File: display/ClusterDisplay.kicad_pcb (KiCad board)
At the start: 4 copper layers, 125.4 x 106 mm, 117 parts, among them J1 Verdin iMX95 Hexa 8GB WB IT, J10 RTC coin cell, J11 Molex KK-254 22-27-2041, rota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, J2 Phoenix MKDS 1,5/3-5,08 power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, J3 Molex KK-254 22-27-2031 priva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, J4 TST040HDBC-42 panel, J8 Samtec TSW-108-07-G-S JTAG (b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, J9 Samtec TSW-104-07-G-S buttons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, Q1 PMV55ENEA (AEC-Q101, 60V/20V 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, Q2 PMV55ENEA (AEC-Q101, 60V/20V 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, Q3 PMV55ENEA ignition wake pulld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, U1 LM74930-Q1, U2 LM61460-Q1, U3 TLV767-Q1, U4 TCAN1044V-Q1, U6 TPS65131-Q1, U7 TPS61165-Q1, U8 TPS22918-Q1 (AEC-Q100 G2) dia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

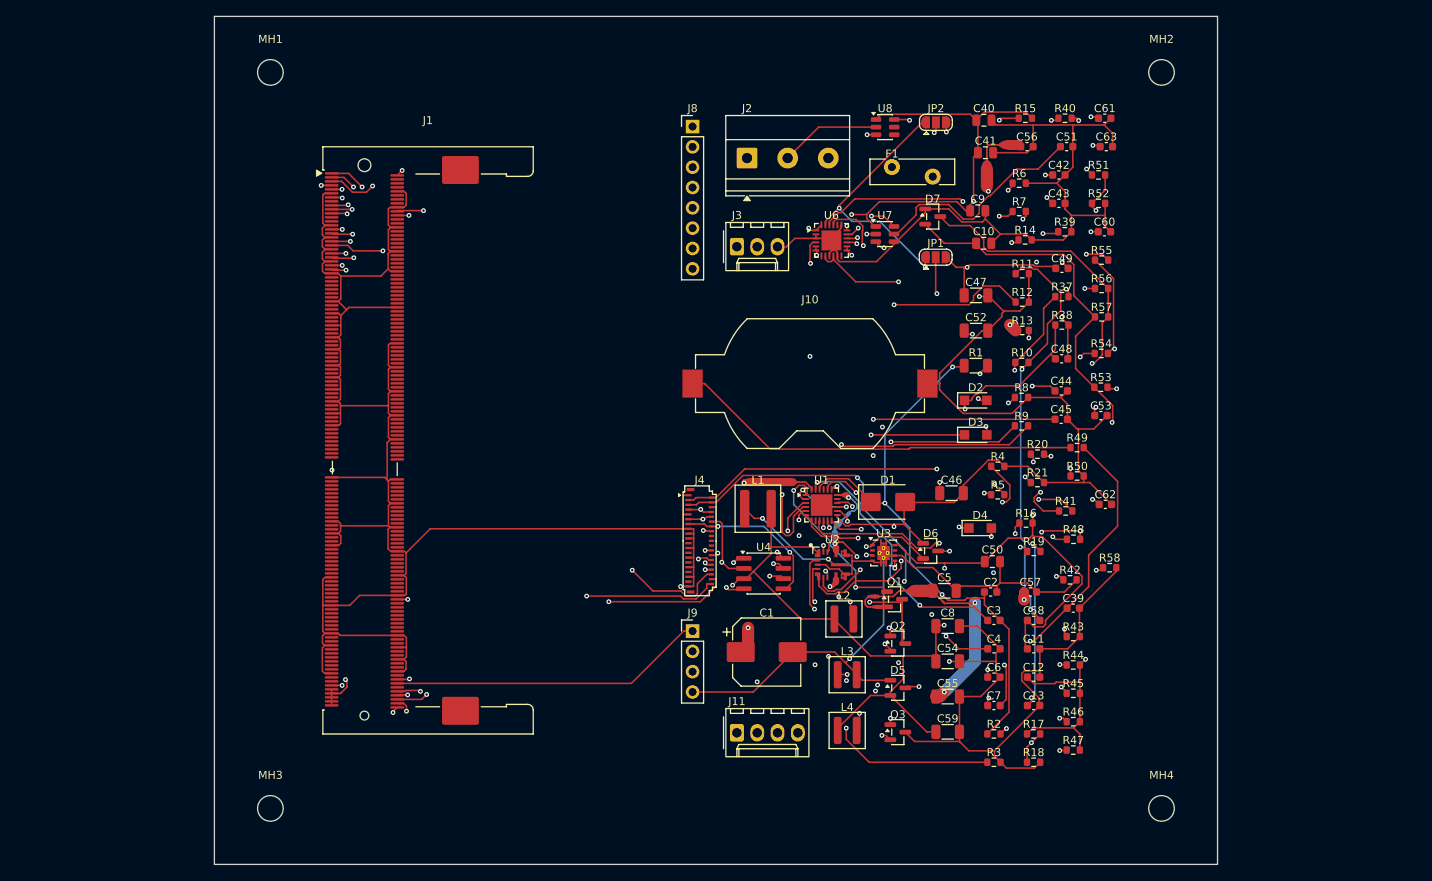
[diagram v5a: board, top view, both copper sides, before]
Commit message: Fix review findings: MOSFET pinout, gauges surge front end, converter cells, DSI
Review of 2026-10-03 found real defects; fixes and measured results:
- Nexperia PMV55ENEA/PMV37ENEA pinout is G=1, S=2, D=3: display Q1-Q3 and
  gauges Q2 had source/drain swapped. Fixed in both schematics.
- gauges/ now has the same LM74930-Q1 surge-protected front end as display/
  (5 mohm sense, OV clamp), a 5 A/32 V blade fuse on display/ (the MF-RG500 PTC
  was a 16 V part), and sender inputs with series resistor, clamp and filter.
- Converters are placed as cells around their ICs (tools/cellplace.py).
  display: SW_5V 55.6 -> 11.6 mm, boost/inverter/backlight SW 75 -> 7-13 mm,
  LM61460 input caps 57 -> 4.7-7.5 mm. gauges: SW 26.8 -> 8.7 mm, input caps 4.5 mm.
- display DSI pairs are planned by dsi_route.py after the autorouter: legs
  10.6-11.2 mm, at most 0.6 mm skew in a pair (was 64-85 mm, 21 mm skew).
- In1 is a GND plane for the router on display/ (about 925 mm of slow signals
  still cross it, down from 2615); forbidding signals there left 6-122
  connections unrouted. gauges/ keeps the old flow (planes claimed there made
  the real GND zone split into islands).
- display: USB (J13) and console UART (J12) bring-up headers, SoM and socket
  split into separate BOM lines, README rewritten.
- gauges: orderable MCU part number, DNP parts get their own BOM line and are
  left out of the placement file, 5 mohm sense resistor in the catalog.

Both boards: 0 unconnected, independent kicad-cli DRC with only accepted
categories; fab packages rebuilt. Nothing is fabricated or tested.

Co-Authored-By: Claude Sonnet 5.5 <noreply@anthropic.com>
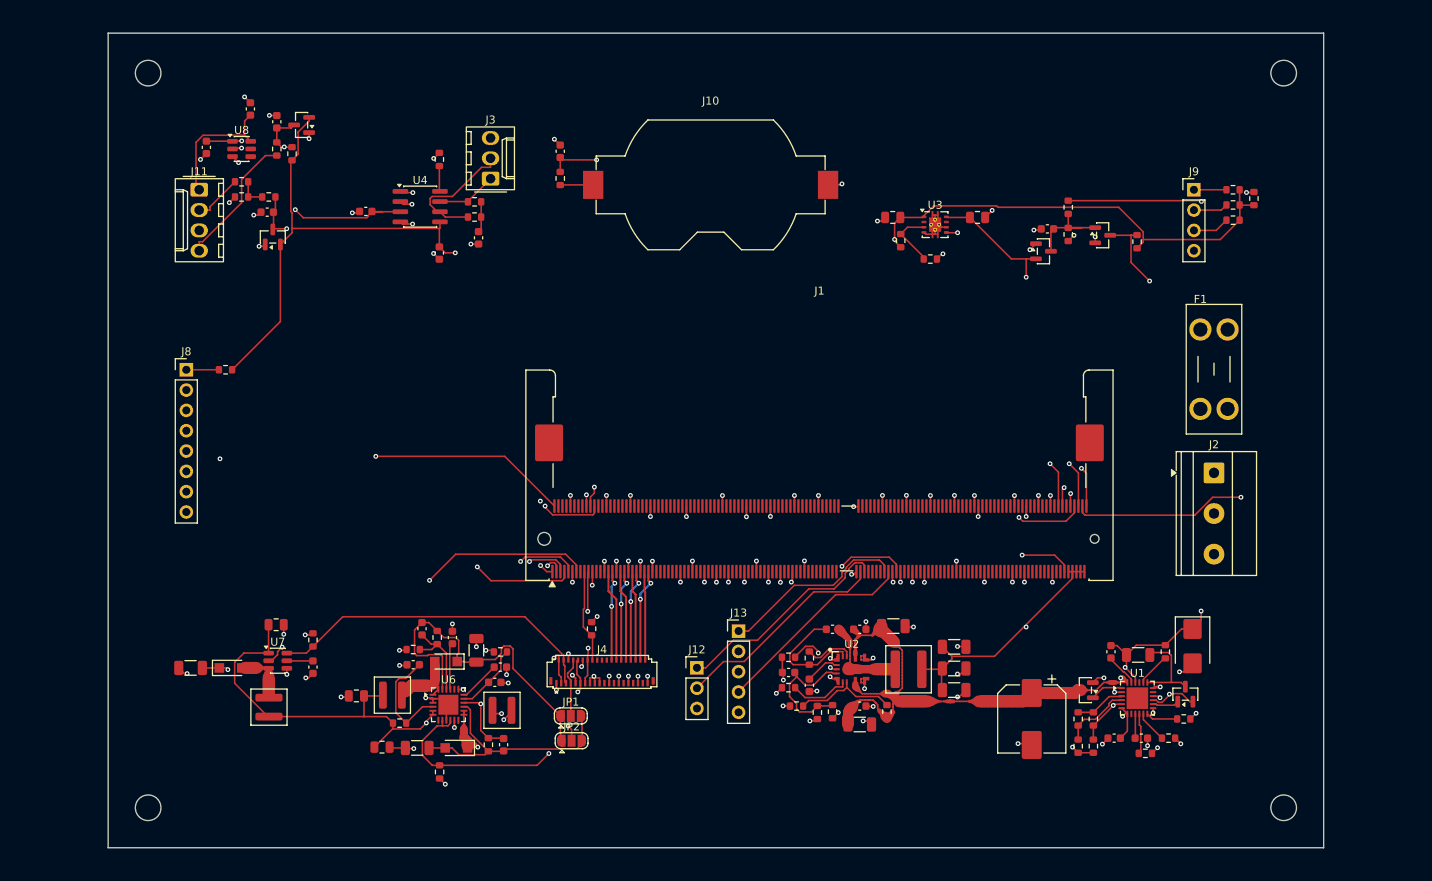
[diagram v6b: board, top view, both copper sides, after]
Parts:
- added J12: Samtec TSW-103-07-G-S A55 console UART_3 1.8V (bench only), Connector_PinHeader_2.54mm:PinHeader_1x03_P2.54mm_Vertical, F.Cu at (207.6, 176.9)
- added J13: Samtec TSW-105-07-G-S USB_1 OTG (bench only), Connector_PinHeader_2.54mm:PinHeader_1x05_P2.54mm_Vertical, F.Cu at (212.8, 172.3)
- F1: value MF-RG500 (Bourns, 5.0A hold/8.5A trip, AEC-Q200) -> Keystone 3568 holder, 5A Littelfuse 0297005.WXNV MINI blade fuse (32V, 1kA); footprint Fuse:Fuse_Bourns_MF-RG500 -> Fuse:Fuseholder_Blade_Mini_Keystone_3568
- moved R58 118.0 mm to (150.7, 118.1), turned to 180 degrees
- moved C51 114.5 mm to (159.6, 176.8), turned to -90 degrees
- moved C62 114.1 mm to (155.1, 108.7), turned to 90 degrees
- moved C60 112.8 mm to (146.3, 111.9), turned to -90 degrees
- moved R54 109.6 mm to (150.7, 116.2)
- moved R48 108.1 mm to (148.7, 139.7)
- moved C63 107.1 mm to (151.8, 107.1), turned to 90 degrees
- moved C52 106.8 mm to (144.3, 176.9), turned to 180 degrees
- moved C40 106.4 mm to (165.1, 180.4), turned to 180 degrees
- moved R40 106.4 mm to (181.6, 186.5), turned to 90 degrees
- moved C41 105.9 mm to (168.3, 186.8)
- moved C61 105.3 mm to (153.9, 120.0), turned to 180 degrees
- moved R56 104.6 mm to (155.1, 112.1), turned to 90 degrees
- moved R55 104.4 mm to (154.1, 118.1)
- moved R57 103.2 mm to (157.0, 112.7), turned to 90 degrees
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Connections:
- J1 pad 147: (no net) -> UART_RXD
- J1 pad 149: (no net) -> UART_TXD
- J1 pad 159: (no net) -> USB_VBUS
- J1 pad 161: (no net) -> USB_ID
- J1 pad 163: (no net) -> USB_DN
- J1 pad 165: (no net) -> USB_DP
- Q1 pad 2: +12V_PROT -> COMMON
- Q1 pad 3: COMMON -> +12V_PROT
- Q2 pad 2: SENSE_OUT -> COMMON
- Q2 pad 3: COMMON -> SENSE_OUT
- Q3 pad 2: IGN_WAKE_N -> GND
- Q3 pad 3: GND -> IGN_WAKE_N
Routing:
- net GND: track 760.2 -> 156.8 mm, vias 6 -> 120
- net +12V_PROT: track 190.1 -> 72.9 mm, vias 11 -> 2
- net DIAL_ADC: track 171.7 -> 63.8 mm, vias 4 -> 2
- net DSI_PANEL_EN: track 116.2 -> 11.6 mm, vias 3 -> 0
- net PANEL_BIAS_EN: track 149.8 -> 49.3 mm, vias 4 -> 2
- net DIAL_5V: track 113.1 -> 16.4 mm, vias 2 -> 0
- net DIAL_SIG_RAW: track 86.2 -> 6.18 mm, vias 2 -> 0
- net IGN_WAKE_N: track 122.1 -> 42.3 mm, vias 3 -> 2
- net JTAG_VREF: track 142.1 -> 63.2 mm, vias 3 -> 1
- net DSI_D2_N: track 85.4 -> 11.0 mm, vias 3 -> 0
- net CAN1_H: track 80.6 -> 7.58 mm, vias 2 -> 0
- net CAN1_L: track 88.5 -> 16.4 mm, vias 2 -> 0
- net IGN_GATE: track 83.4 -> 11.6 mm, vias 4 -> 0
- net BL_SW: track 76.6 -> 7.06 mm, vias 3 -> 0
- net PANEL_FBN: track 84.8 -> 16.8 mm, vias 4 -> 2
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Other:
- board size 125.4 x 106 mm -> 151.9 x 101.8 mm

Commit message: display: audio path, USB-C host port and wireless-radio notes for wireless Android Auto / CarPlay
Owner decision 2026-10-16: wireless Android Auto and CarPlay with sound.

- Audio: TI TAC5112-Q1 codec (real datasheet SLASFC2A, 1.8 V I/O so no level
  shifters, no MCLK) on Verdin I2S_1 + I2C_1, 3.3 V AVDD LDO, balanced stereo
  line-out J14, electret mic J15, TPD4E05U06-Q1 ESD, reserved DNP/TBD MFi
  coprocessor access header J16 (no Apple part invented).
- USB: USB-C 2.0 host J17 on Verdin USB_2, TPS2557-Q1 VBUS switch (1.6-2.0 A),
  22k Rp (1.5 A), ESD, VBUS TVS, EN pull-down. J13 stays the bench header.
- verdin_x1: I2S_1, I2C_1 and USB_2 moved out of the unused bank; verify() updated.
- Floorplan: audio column in the left strip, connector/ESD cell leads the top
  row, USB-C cell on the bottom edge. 151.9 -> 169.3 mm wide, same height.
- Routing: 0 unconnected nets (real kicad-cli DRC); B.Cu GND pour added to stop
  In1 islands from isolating GND vias; in-place retries cut, pipeline retries up.
- cellplace: optional keepin and anchor_gap per cell.
- BOM, fab package, README, fab README, PLAN decision 6 and docs/audio-and-usb.md
  (wiring, unbalanced AUX use, antenna rules, software bring-up, unverified list).

Co-Authored-By: Claude Sonnet 5.5 <noreply@anthropic.com>
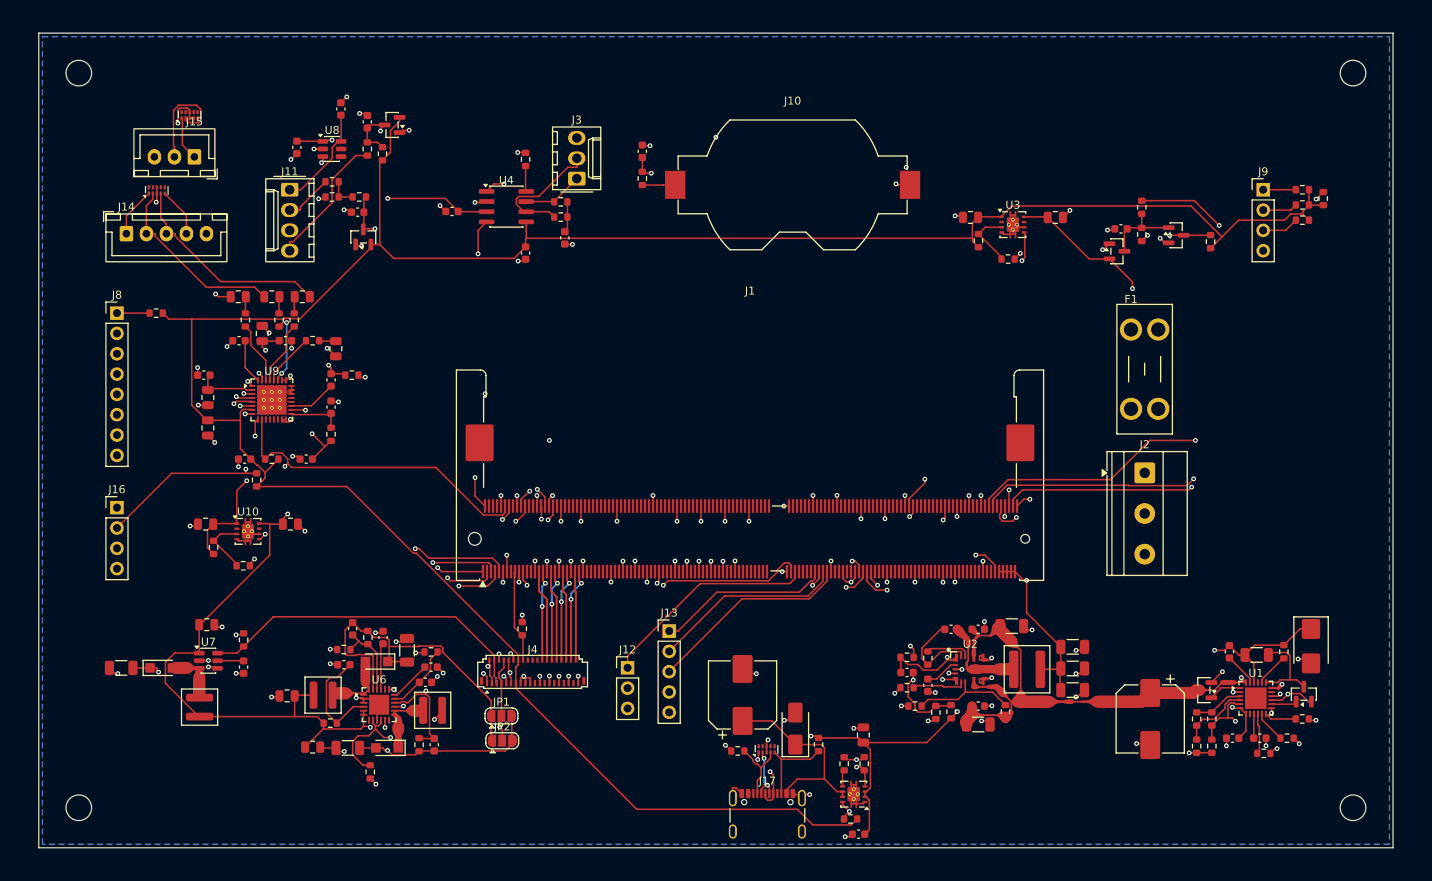
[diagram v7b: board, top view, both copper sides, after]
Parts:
- added C64: 10u CIN, Capacitor_SMD:C_0805_2012Metric, F.Cu at (156.8, 159.0)
- added C65: 10u COUT, Capacitor_SMD:C_0805_2012Metric, F.Cu at (146.2, 159.0)
- added C66: 10u AVDD, Capacitor_SMD:C_0805_2012Metric, F.Cu at (153.3, 135.1)
- added C67: 100n AVDD, Capacitor_SMD:C_0603_1608Metric, F.Cu at (156.2, 136.0)
- added C68: 10u DREG, Capacitor_SMD:C_0805_2012Metric, F.Cu at (146.5, 143.1)
- added C69: 100n DREG, Capacitor_SMD:C_0603_1608Metric, F.Cu at (146.0, 140.3)
- added C70: 10u IOVDD, Capacitor_SMD:C_0805_2012Metric, F.Cu at (146.5, 146.9)
- added C71: 100n IOVDD, Capacitor_SMD:C_0603_1608Metric, F.Cu at (151.1, 150.8)
- added C72: 1u VREF, Capacitor_SMD:C_0603_1608Metric, F.Cu at (150.4, 136.0)
- added C73: 1u MICBIAS, Capacitor_SMD:C_0603_1608Metric, F.Cu at (161.9, 144.3)
- added C74: 1u mic AC couple, Capacitor_SMD:C_0603_1608Metric, F.Cu at (158.8, 150.8)
- added C75: 1u mic AC couple, Capacitor_SMD:C_0603_1608Metric, F.Cu at (161.9, 140.9)
- added C76: 4.7u line-out DC block, Capacitor_SMD:C_0805_2012Metric, F.Cu at (162.5, 137.0)
- added C77: 4.7u line-out DC block, Capacitor_SMD:C_0805_2012Metric, F.Cu at (154.5, 130.5)
- added C78: 4.7u line-out DC block, Capacitor_SMD:C_0805_2012Metric, F.Cu at (158.3, 130.5)
- added C79: 4.7u line-out DC block, Capacitor_SMD:C_0805_2012Metric, F.Cu at (150.3, 130.5)
- added C80: 100n USB switch IN, Capacitor_SMD:C_0603_1608Metric, F.Cu at (227.8, 197.7)
- added C81: 10u USB switch IN, Capacitor_SMD:C_0805_2012Metric, F.Cu at (228.4, 185.3)
- added C82: 100u 35V hybrid polymer VBUS (Panasonic EEH-ZA1V101P), Capacitor_SMD:CP_Elec_8x10, F.Cu at (213.3, 180.3)
- added D8: SMAJ5.0A VBUS TVS, Diode_SMD:D_SMA, F.Cu at (219.9, 184.5)
- added J14: JST XH B5B-XH-A balanced line-out L/R, Connector_JST:JST_XH_B5B-XH-A_1x05_P2.50mm_Vertical, F.Cu at (136.3, 122.7)
- added J15: JST XH B3B-XH-A electret microphone (2-wire + shield), Connector_JST:JST_XH_B3B-XH-A_1x03_P2.50mm_Vertical, F.Cu at (144.8, 113.1)
- added J16: MFi coprocessor access I2C_1 + reset (TBD, DNP), Connector_PinHeader_2.54mm:PinHeader_1x04_P2.54mm_Vertical, F.Cu at (135.1, 156.9)
- added J17: GCT USB4105-GF-A USB-C 2.0 host receptacle, Connector_USB:USB_C_Receptacle_GCT_USB4105-xx-A_16P_TopMnt_Horizontal, F.Cu at (216.4, 196.3)
- added R59: 316k 1% FB top, Resistor_SMD:R_0603_1608Metric, F.Cu at (147.2, 161.9)
- added R60: 100k FB bot, Resistor_SMD:R_0603_1608Metric, F.Cu at (150.9, 164.2)
- added R61: 2.2k I2C1 SDA pull-up, Resistor_SMD:R_0603_1608Metric, F.Cu at (154.5, 150.8)
- added R62: 2.2k I2C1 SCL pull-up, Resistor_SMD:R_0603_1608Metric, F.Cu at (152.6, 153.4)
- added R63: 2.2k mic bias, Resistor_SMD:R_0603_1608Metric, F.Cu at (161.9, 147.7)
- added R64: 100R mic return, Resistor_SMD:R_0603_1608Metric, F.Cu at (164.5, 140.3)
- added R65: 100R line-out series, Resistor_SMD:R_0603_1608Metric, F.Cu at (159.6, 136.0)
- added R66: 100R line-out series, Resistor_SMD:R_0603_1608Metric, F.Cu at (155.4, 133.4)
- added R67: 100R line-out series, Resistor_SMD:R_0603_1608Metric, F.Cu at (157.3, 133.4)
- added R68: 100R line-out series, Resistor_SMD:R_0603_1608Metric, F.Cu at (151.2, 133.4)
- added R69: 61.9k 1% USB ILIM (1.6-2.0 A), Resistor_SMD:R_0603_1608Metric, F.Cu at (226.0, 188.9)
- added R70: 100k FAULT pull-up to +1V8, Resistor_SMD:R_0603_1608Metric, F.Cu at (226.8, 195.8)
- added R71: 22k Rp CC1 (1.5 A, +/-5 percent or better), Resistor_SMD:R_0603_1608Metric, F.Cu at (212.7, 187.3)
- added R72: 22k Rp CC2 (1.5 A, +/-5 percent or better), Resistor_SMD:R_0603_1608Metric, F.Cu at (222.8, 186.5)
- added R73: 100k USB EN pull-down, Resistor_SMD:R_0603_1608Metric, F.Cu at (228.5, 188.9)
- added U10: TLV767-Q1 (3.3 V audio AVDD), Package_DFN_QFN:Texas_DRB0008A, F.Cu at (151.5, 159.9)
- added U11: TPS2557-Q1, Package_DFN_QFN:Texas_DRB0008A, F.Cu at (227.2, 192.7)
- added U12: TPD4E05U06-Q1 line-out ESD, Package_SON:USON-10_2.5x1.0mm_P0.5mm, F.Cu at (140.1, 117.3)
- added U13: TPD4E05U06-Q1 mic ESD, Package_SON:USON-10_2.5x1.0mm_P0.5mm, F.Cu at (144.2, 107.9)
- added U14: TPD4E05U06-Q1 USB ESD, Package_SON:USON-10_2.5x1.0mm_P0.5mm, F.Cu at (216.3, 187.1)
- added U9: TAC5112-Q1, Package_DFN_QFN:QFN-32-1EP_5x5mm_P0.5mm_EP3.7x3.7mm_ThermalVias, F.Cu at (154.5, 143.4)
- moved C1 14.8 mm to (264.3, 183.3)
- moved C2 14.8 mm to (274.6, 185.7)
- moved C3 14.8 mm to (274.2, 174.9)
- moved C4 14.8 mm to (278.0, 185.7)
- moved C5 14.8 mm to (242.8, 184.0)
- moved C54 14.8 mm to (254.6, 177.0)
- moved C55 14.8 mm to (247.0, 171.7)
- moved C56 14.8 mm to (242.8, 181.7)
- moved C57 14.8 mm to (242.8, 172.1)
- moved C59 14.8 mm to (254.6, 174.3)
- moved C6 14.8 mm to (236.5, 179.1)
- moved C8 14.8 mm to (254.6, 179.7)
- moved D1 14.8 mm to (284.4, 174.2)
- moved Q1 14.8 mm to (271.0, 179.7)
- moved Q2 14.8 mm to (283.5, 180.2)
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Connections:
- J1 pad 12: (no net) -> I2C1_SDA
- J1 pad 14: (no net) -> I2C1_SCL
- J1 pad 181: (no net) -> USB2_DN
- J1 pad 183: (no net) -> USB2_DP
- J1 pad 185: (no net) -> USB2_EN
- J1 pad 187: (no net) -> USB2_OC_N
- J1 pad 208: (no net) -> MFI_RST_N
- J1 pad 30: (no net) -> I2S_BCLK
- J1 pad 32: (no net) -> I2S_FSYNC
- J1 pad 34: (no net) -> I2S_DIN
- J1 pad 36: (no net) -> I2S_DOUT
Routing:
- net MFI_RST_N: track 0.00 -> 103.2 mm, vias 0 -> 1
- net PWR_EN_MOCI: track 48.6 -> 133.7 mm, vias 2 -> 3
- net I2C1_SCL: track 0.00 -> 84.7 mm, vias 0 -> 3
- net +1V8: track 233.7 -> 312.1 mm, vias 3 -> 0
- net I2C1_SDA: track 0.00 -> 63.5 mm, vias 0 -> 1
- net GND: track 156.8 -> 217.6 mm, vias 120 -> 144
- net I2S_DOUT: track 0.00 -> 56.0 mm, vias 0 -> 3
- net MIC_P: track 0.00 -> 54.1 mm, vias 0 -> 1
- net I2S_BCLK: track 0.00 -> 52.1 mm, vias 0 -> 3
- net MIC_N: track 0.00 -> 51.6 mm, vias 0 -> 1
- net I2S_FSYNC: track 0.00 -> 49.2 mm, vias 0 -> 2
- net I2S_DIN: track 0.00 -> 47.4 mm, vias 0 -> 2
- net LINE_L_P: track 0.00 -> 38.7 mm, vias 0 -> 1
- net USB2_DP: track 0.00 -> 38.2 mm, vias 0 -> 3
- net USB2_DN: track 0.00 -> 38.2 mm, vias 0 -> 3
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- added copper zone on B.Cu, net GND
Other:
- board size 151.9 x 101.8 mm -> 169.3 x 101.8 mm
